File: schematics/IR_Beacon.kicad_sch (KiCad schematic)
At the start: 30 parts, among them Q3 LTR3208E, Q4 LTR3208E, U11 MCP6294, U12 MCP6294, U13 LM339AN, U14 LM339AN

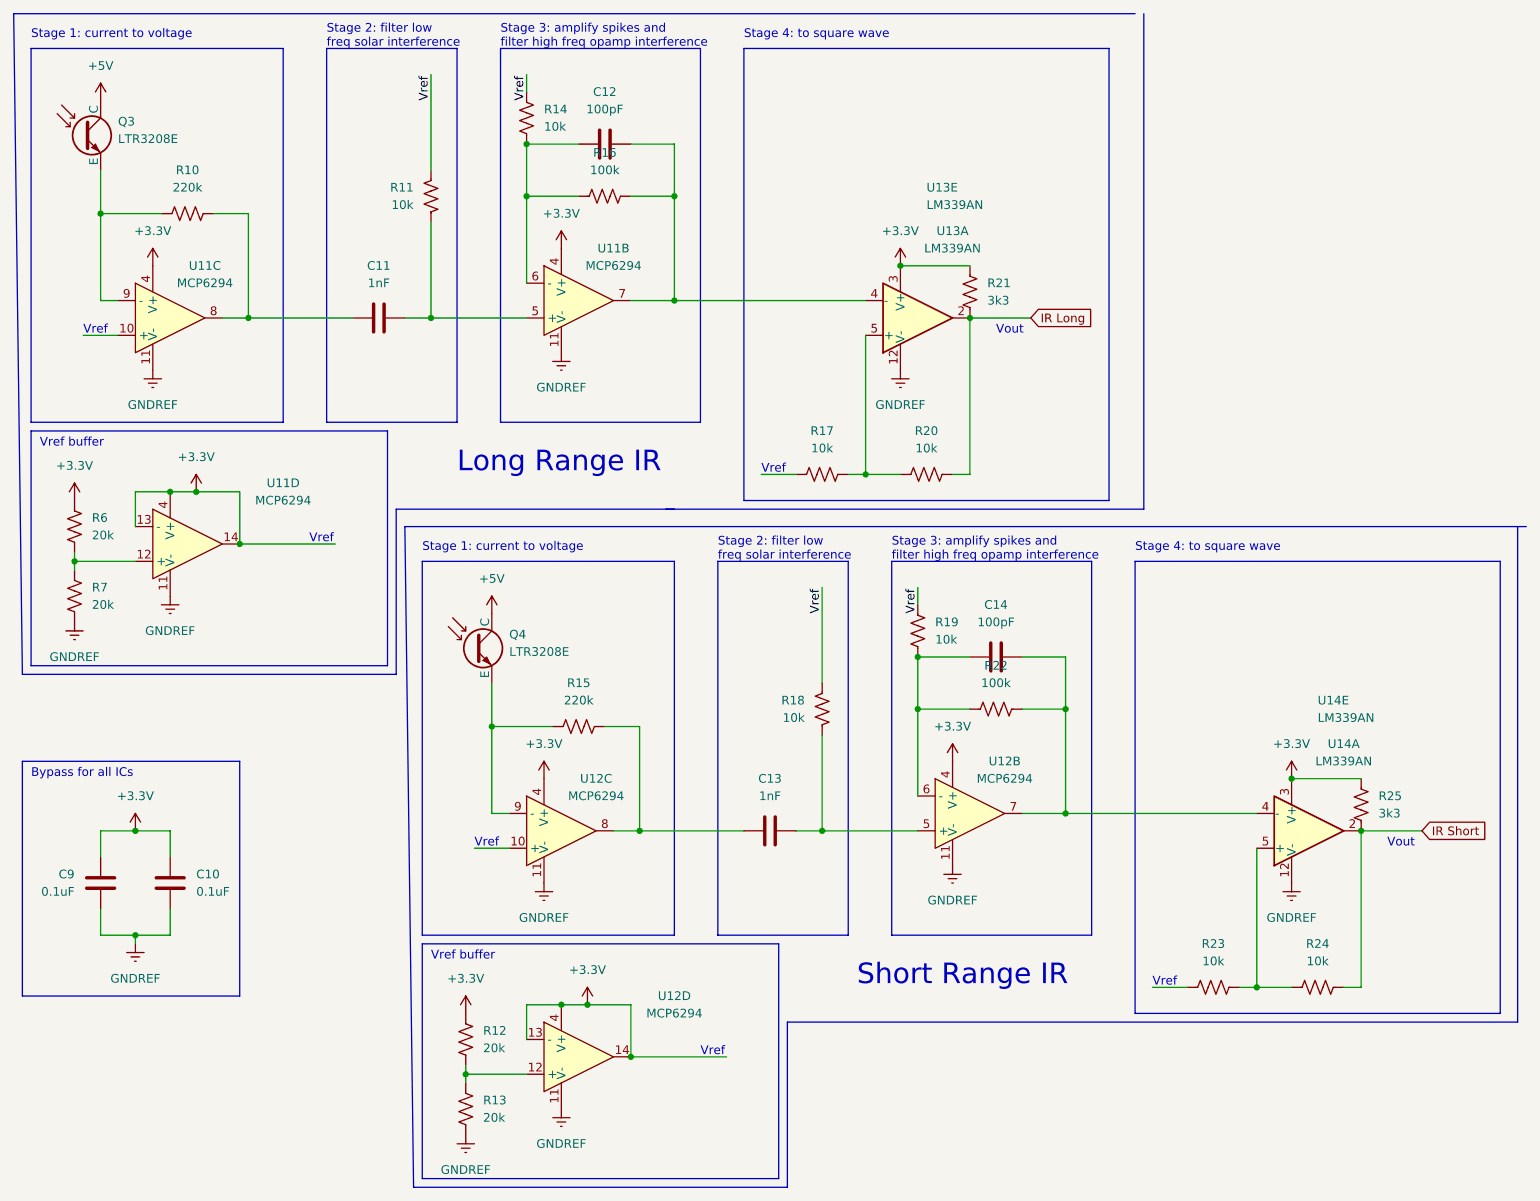
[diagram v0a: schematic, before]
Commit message: Update KiCAD schematic and write getter functions for switches
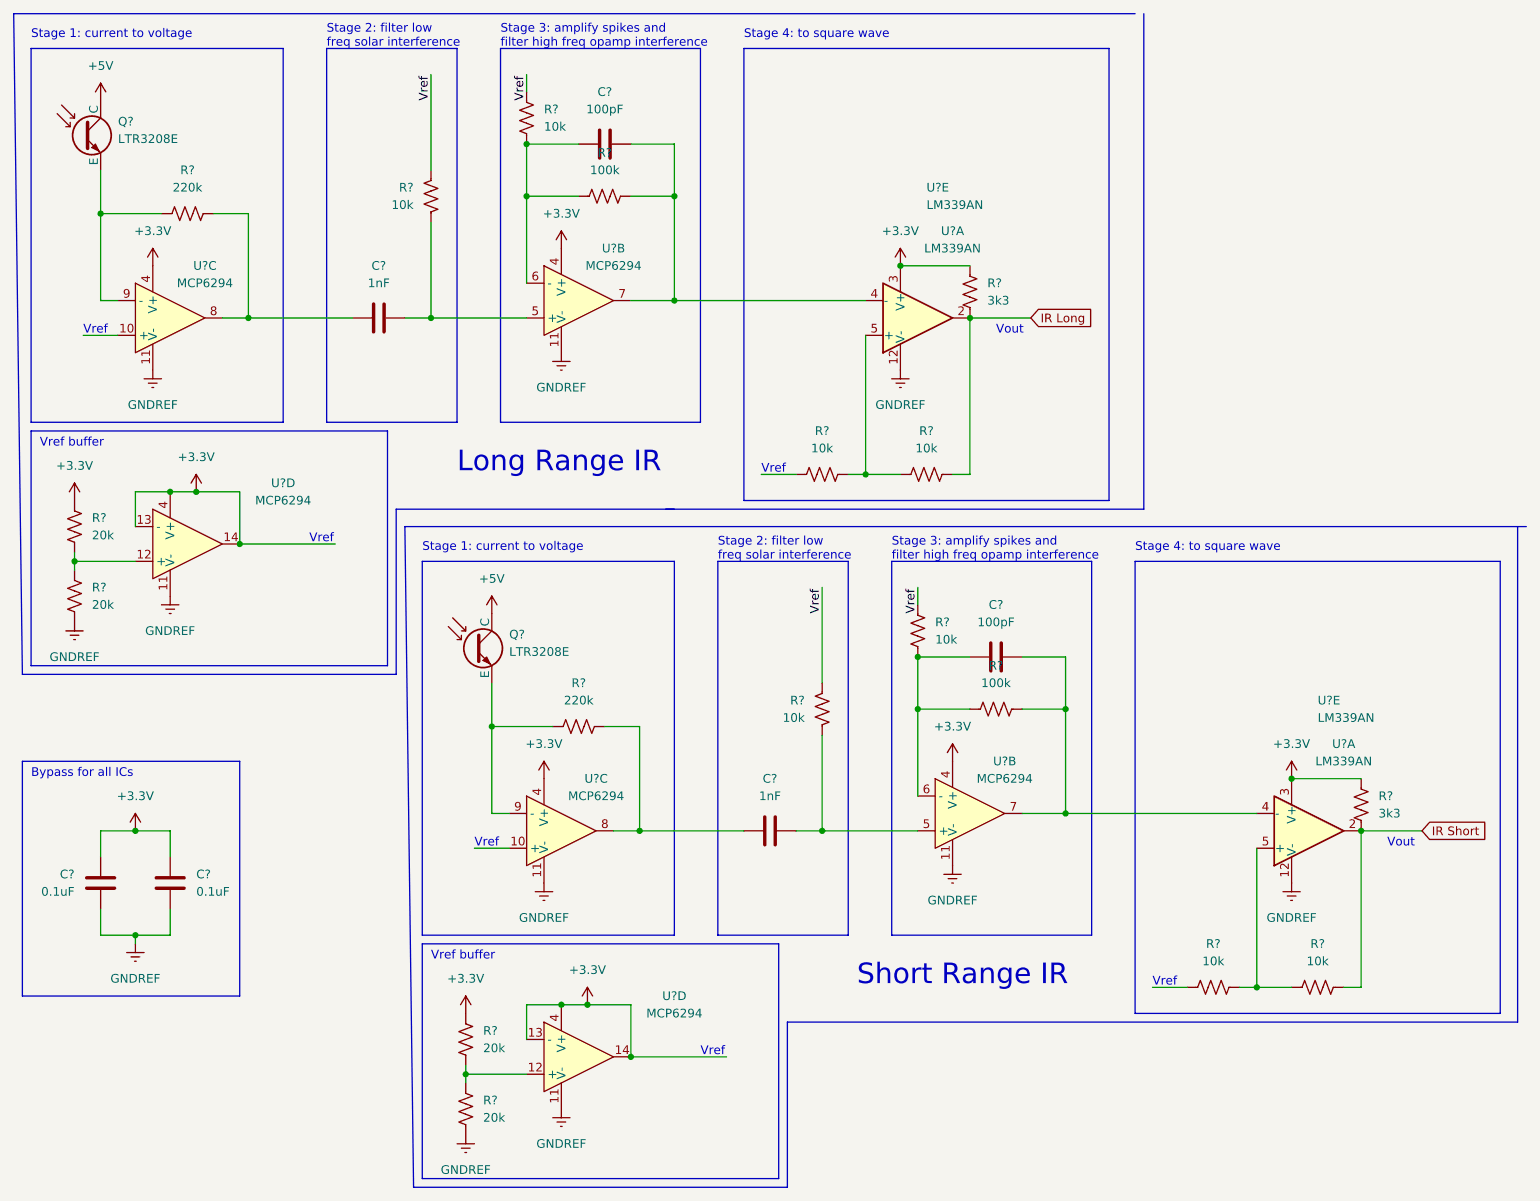
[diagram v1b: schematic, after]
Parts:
- renumbered C13 to C?, C14 to C?, C12 to C?, C9 to C?, C10 to C?, C11 to C?, Q3 to Q?, Q4 to Q?, R25 to R?, R14 to R?, R12 to R?, R17 to R?, R21 to R?, R15 to R?, R20 to R?, R22 to R?, R16 to R?, R7 to R?, R10 to R?, R13 to R?, R24 to R?, R19 to R?, R23 to R?, R11 to R?, R18 to R?, R6 to R?, U14 to U?, U11 to U?, U13 to U?, U12 to U?
